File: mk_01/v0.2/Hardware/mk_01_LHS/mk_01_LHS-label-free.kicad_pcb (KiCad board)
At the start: 2 copper layers, 165.1 x 102.9 mm, 79 parts, among them SW1 SW_Push_Dual, U1 nice_nano

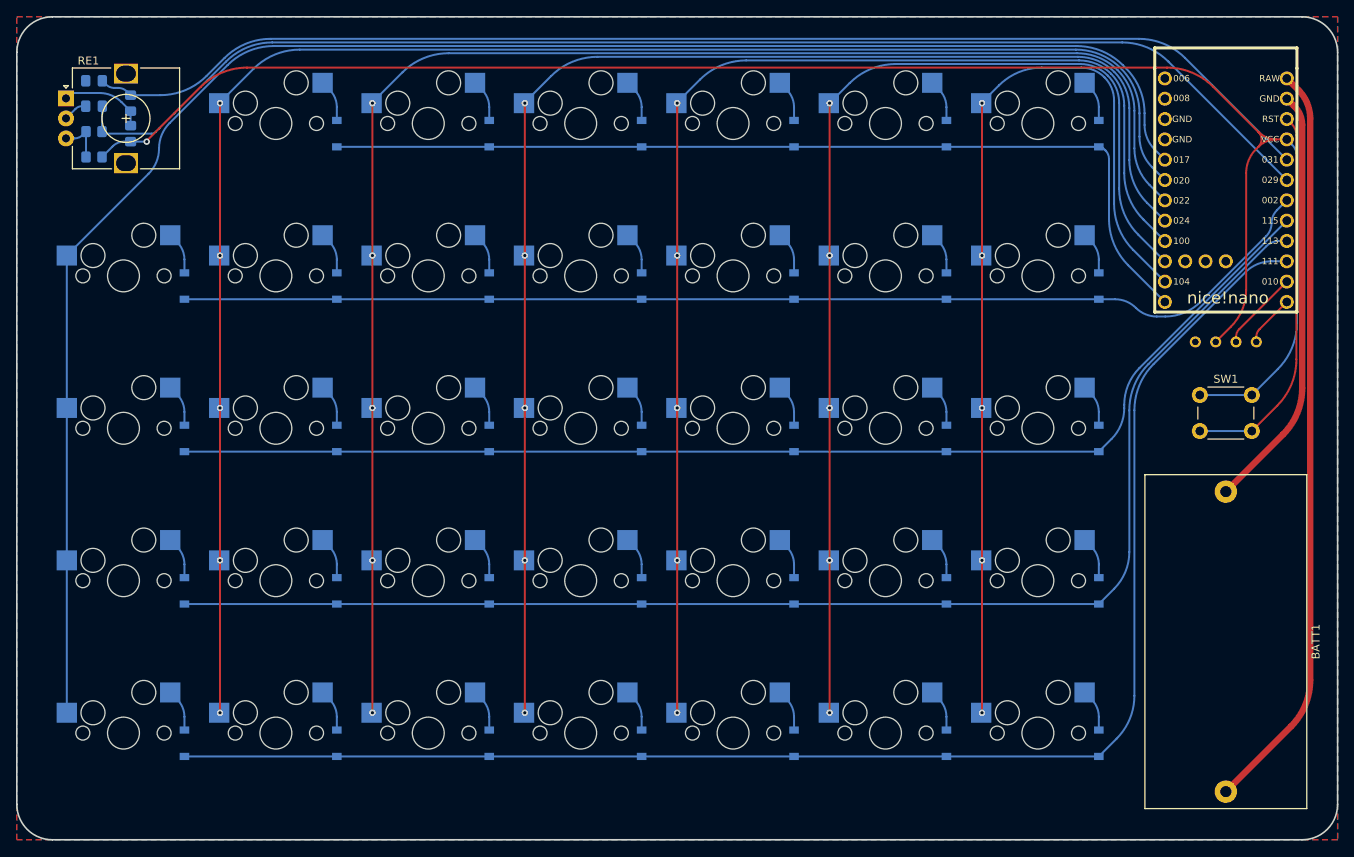
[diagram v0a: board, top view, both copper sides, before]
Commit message: Finalising layout and troubleshooting round-tracks
The layout is pretty much complete, with all necessary components wired correctly. round-tracks keeps refusing to round one of the traces. A label free version has been added, however I'll probably remove this since it means two designs to constantly keep up to date.
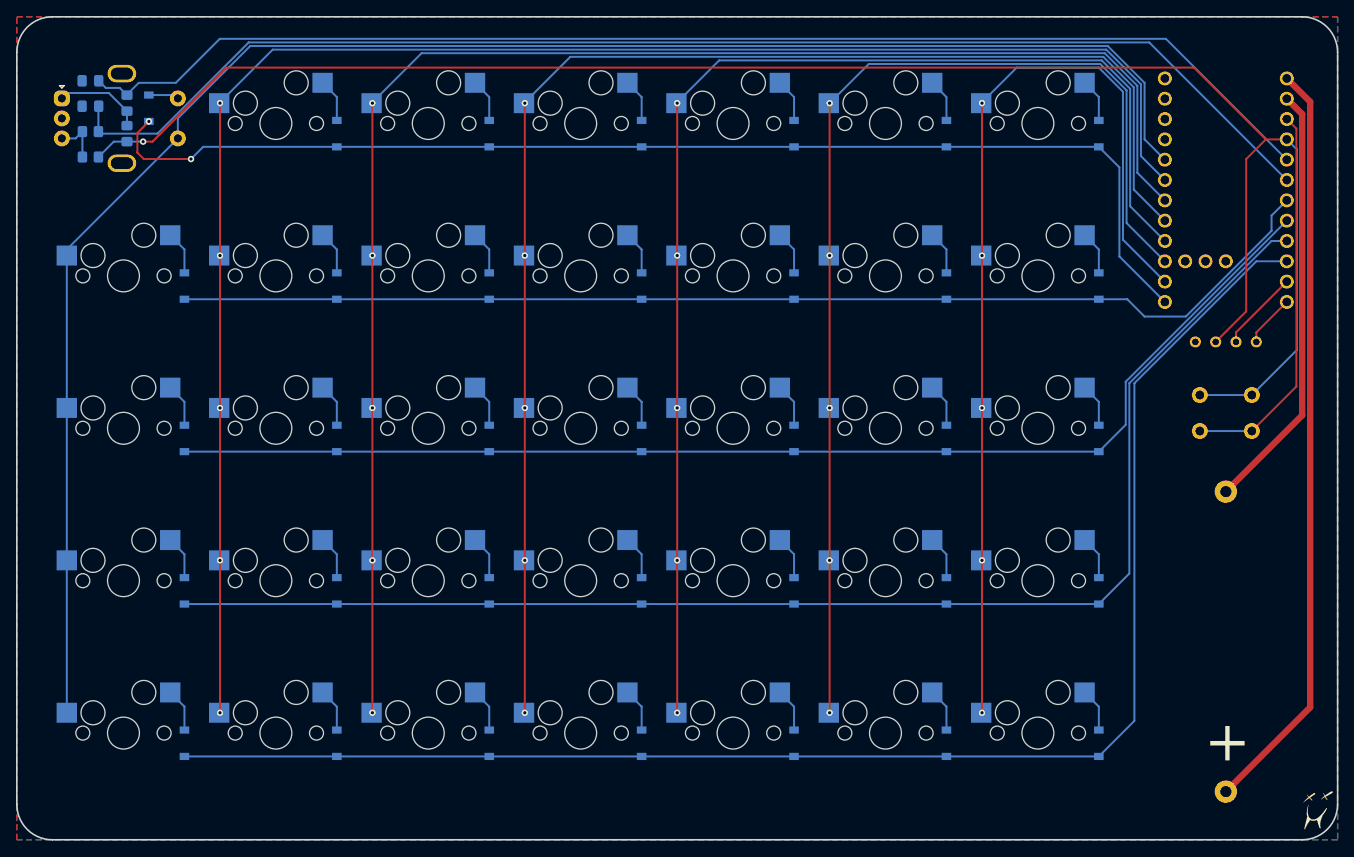
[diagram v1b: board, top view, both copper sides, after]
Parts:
- added D_35: D, Diode_SMD:D_SOD-123, B.Cu at (43.8, 45.1)
- added REF**: Logo, Logos:Logo, F.Cu at (189.9, 132.7)
- added REF**: Logo, Logos:Logo, B.Cu at (188.6, 132.7)
- RE1: value RotaryEncoder -> RotaryEncoder_Switch; footprint Rotary_Encoder:RotaryEncoder_Alps_EC12E_Vertical_H20mm -> Rotary_Encoder:RotaryEncoder_Alps_EC11E-Switch_Vertical_H20mm
- moved RE1 0.52 mm to (32.9, 43.9)
- moved C7 0.45 mm to (36.5, 41.7)
- moved C8 0.45 mm to (36.5, 44.8)
- moved R1 0.45 mm to (41.1, 44.5)
- moved R2 0.45 mm to (41.1, 48.3)
- moved R3 0.45 mm to (36.5, 48.0)
- moved R4 0.45 mm to (36.5, 51.2)
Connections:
- net Net-(C7-Pad2) renamed P0.31
- net Net-(C8-Pad1) renamed P0.29
- U1 pad 4: unconnected-(U1-Pad4) -> Earth
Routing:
- net row0: track 117.8 -> 148.8 mm, vias 0 -> 2
- net Net-(RE1-PadS2): track 0.00 -> 4.53 mm
- net Earth: track 3.04 -> 0.00 mm
- net col5: track 138.5 -> 140.8 mm
- net col0: track 215.4 -> 217.4 mm
- net P0.31: track 156.7 -> 158.5 mm
- net col1: track 207.5 -> 209.2 mm
- net col2: track 190.2 -> 191.9 mm
- net col3: track 173.0 -> 174.7 mm
- net col4: track 155.8 -> 157.4 mm
- net col6: track 121.5 -> 122.9 mm
- net P0.29: track 162.4 -> 163.7 mm
- net row4: track 187.2 -> 188.2 mm
- net row1: track 144.9 -> 145.8 mm
- net row2: track 152.6 -> 153.5 mm
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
